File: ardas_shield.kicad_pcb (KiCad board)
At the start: 2 copper layers, 68.6 x 53.3 mm, 40 parts, among them CON1 SD_Card, IC1 DS1307, P1 CONN_10, P10 CONN_01X03, P2 CONN_8, P3 CONN_8, P4 CONN_ICSP, P5 CONN_6, P6 TTL_COMM, P7 CONN_01X03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

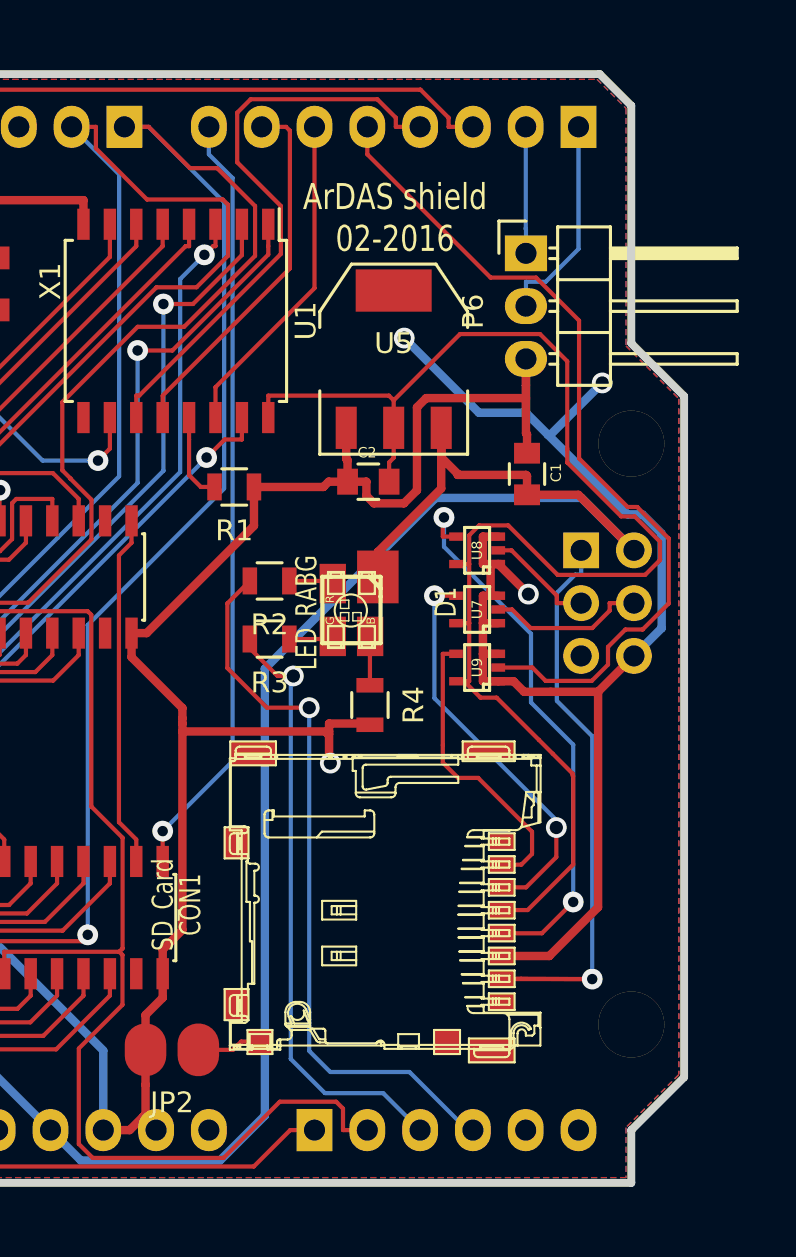
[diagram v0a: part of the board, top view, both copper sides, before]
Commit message: remove SD card and replace led circuit
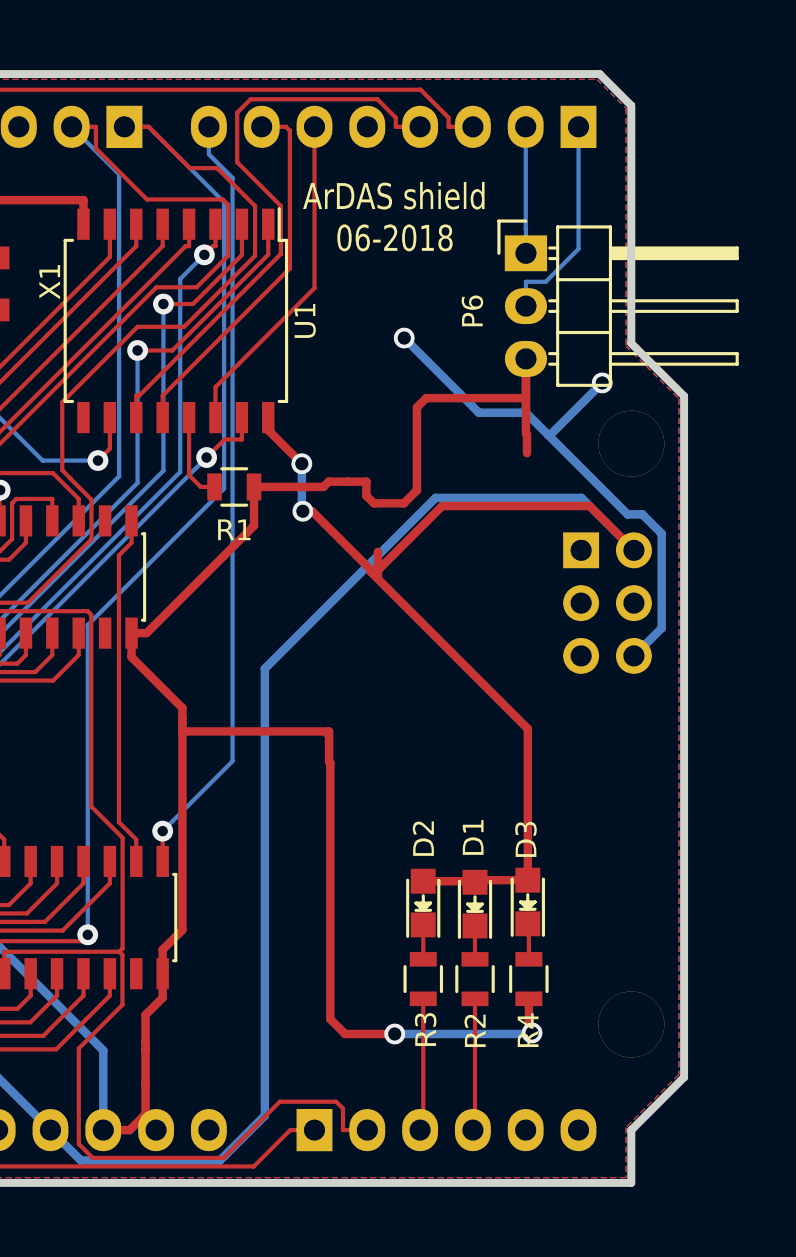
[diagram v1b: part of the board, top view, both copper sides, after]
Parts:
- removed C1, C2: 47uF, kicad-gfa local:C_0805
- removed CON1: SD_Card, kicad-gfa local:microSD_socket
- removed JP2: Jumper_NO_Small, kicad-gfa local:small_no_jumper
- removed U5: LD1117S33TR, kicad-gfa local:SOT-223
- removed U7, U8, U9: 74LVC1G125, kicad-gfa local:SC-70-5
- added D2: LED, kicad-gfa local:LED-0805, F.Cu at (103.1, 108.1)
- added D3: LED, kicad-gfa local:LED-0805, F.Cu at (108.1, 108.0)
- D1: value LED_RABG -> LED; footprint kicad-gfa local:led-P-LCC-4-3 -> kicad-gfa local:LED-0805
- R2: value 4.7k -> 150 Ohm
- R3: value 10k -> 150 Ohm
- R4: value 4.7k -> 160 Ohm
- moved R2 21.6 mm to (105.6, 111.7), turned to 270 degrees
- moved R3 18.0 mm to (103.1, 111.7), turned to 270 degrees
- moved D1 15.3 mm to (105.6, 108.1), turned to 90 degrees
- moved R4 15.2 mm to (108.2, 111.7)
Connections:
- D1 pad 1: +5V -> Net-(D1-Pad1)
- D1 pad 2: Net-(D1-Pad2) -> +5V
- P3 pad 5: D04 -> (no net)
- P4 pad 1: MISO -> (no net)
- P4 pad 3: SCK -> (no net)
- P4 pad 4: MOSI -> (no net)
- R2 pad 1: Net-(D1-Pad4) -> Net-(D1-Pad1)
- R3 pad 1: Net-(D1-Pad3) -> Net-(D2-Pad1)
- R4 pad 1: Net-(D1-Pad2) -> Net-(D3-Pad1)
- U1 pad 16: +3.3V -> +5V
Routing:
- net +3.3V: track 68.6 -> 0.00 mm
- net D04: track 41.0 -> 0.00 mm
- net MISO: track 30.7 -> 0.00 mm, vias 1 -> 0
- net D17: track 35.3 -> 6.61 mm, vias 1 -> 0
- net +5V: track 239.7 -> 267.7 mm, vias 3 -> 5
- net /SCK3: track 26.7 -> 0.00 mm, vias 2 -> 0
- net D16: track 29.7 -> 6.88 mm, vias 1 -> 0
- net /MOSI3: track 19.3 -> 0.00 mm, vias 2 -> 0
- net GND: track 340.8 -> 322.7 mm
- net /SEN3: track 14.3 -> 0.00 mm
- net MOSI: track 7.61 -> 0.00 mm
- net SCK: track 5.25 -> 0.00 mm
- net Net-(CON1-PadCD1): track 3.13 -> 0.00 mm
- net Net-(D1-Pad2): track 2.57 -> 0.00 mm
- net Net-(D1-Pad4): track 2.14 -> 0.00 mm
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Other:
- board text added: "ArDAS shield 06-2018"
- board text removed: "ArDAS shield 02-2016"

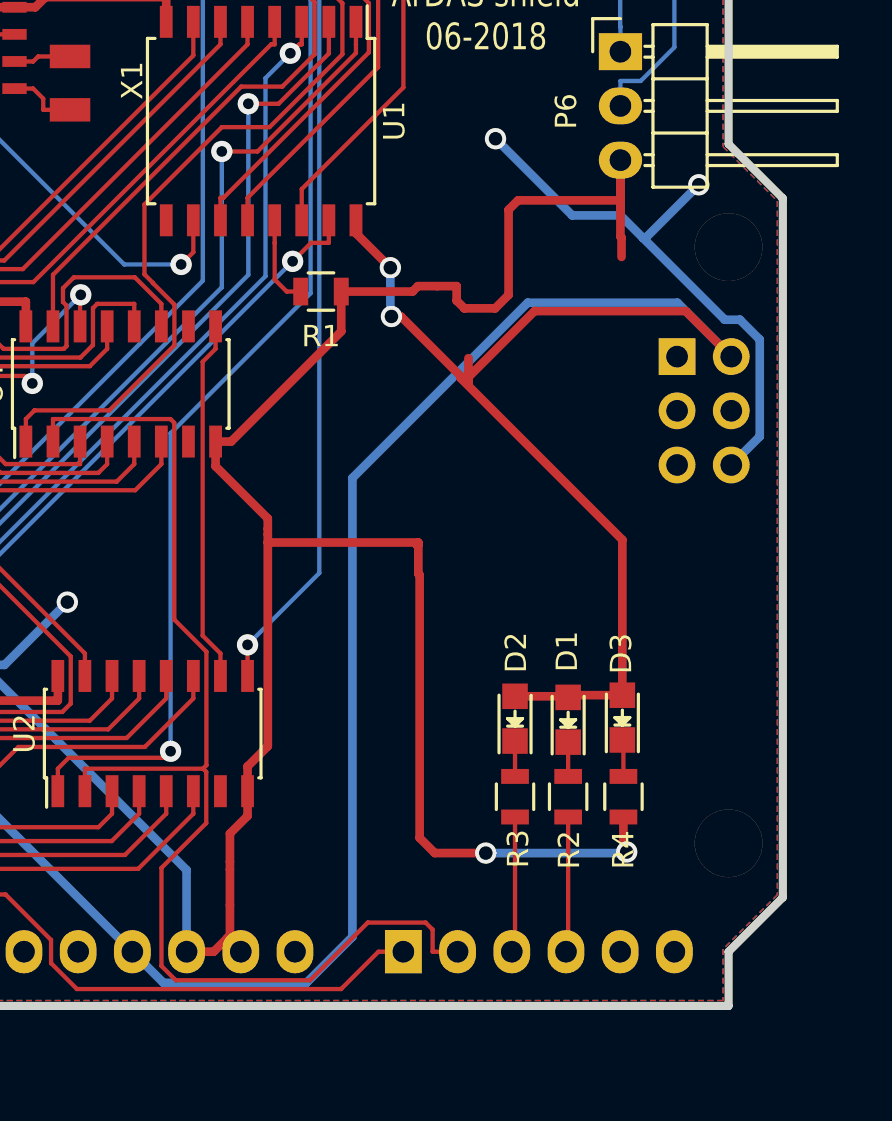
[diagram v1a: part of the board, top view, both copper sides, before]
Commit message: remove ICSP connections from PCB
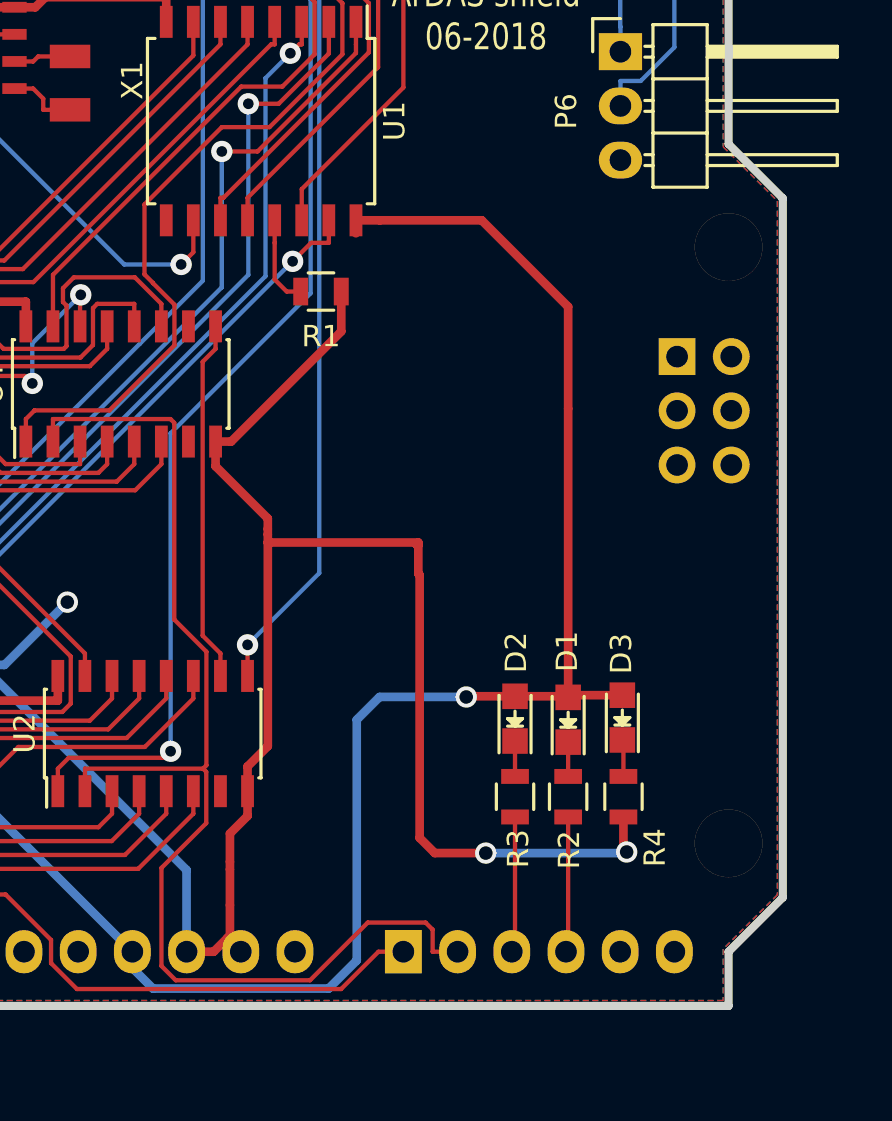
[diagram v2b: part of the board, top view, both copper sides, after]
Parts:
- D2: value LED -> LED Yellow
- D3: value LED -> LED Red
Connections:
- P4 pad 2: +5V -> (no net)
- P4 pad 6: GND -> (no net)
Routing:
- net GND: track 322.7 -> 270.8 mm, vias 12 -> 10
- net +5V: track 267.7 -> 229.7 mm, vias 5 -> 4
